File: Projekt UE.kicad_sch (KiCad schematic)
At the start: 62 parts, among them J1 NEB_21_R, J2 502382-0670, J3 TB006-508-12BE, J4 1935187, J5 215297-8, K1 G5LE-14 DC3, K2 G5LE-14 DC3, K3 G5LE-14 DC3, K4 G5LE-14 DC3, K5 G5LE-14 DC3, Q1 MMBT3904, Q2 MMBT3904, Q3 MMBT3904, Q4 MMBT3904, Q5 MMBT3904, SW1 SW_Push, SW2 SW_Push, SW3 SW_Push, SW4 SW_Push, SW5 SW_Push, SW6 SW_Push, U1 K815P, U2 MIC4575-3.3WU-TR, U3 K845P, U4 STM32F303K8T6, U5 ESP-12E, U6 L7824, Y1 ABM3-8.000MHZ-D2Y-T

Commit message: Update project.
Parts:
- removed K1, K2, K3, K4, K5: G5LE-14 DC3, Relay_THT:Relay_SPDT_Omron-G5LE-1, symbol Relay:G5LE-1
- removed U6: L7824, Package_TO_SOT_THT:TO-220-3_Vertical, symbol Regulator_Linear:L7824
- added K1, K2, K3, K4, K5: V23061B1007A301, SnapEDA Library:RELAY_1-1393223-7, symbol V23061B1007A301:V23061B1007A301
- added R18, R19, R20, R21, R22, R23: 560R, Resistor_SMD:R_1206_3216Metric, symbol Device:R
- C1, C2, C7, C8: footprint (none) -> Capacitor_THT:CP_Radial_D8.0mm_P3.50mm
- C10: footprint (none) -> Capacitor_THT:CP_Radial_D5.0mm_P2.00mm
- C3, C4: footprint (none) -> Capacitor_THT:C_Disc_D6.0mm_W2.5mm_P5.00mm
- C5, C6, C9: footprint (none) -> Capacitor_THT:C_Disc_D10.5mm_W5.0mm_P5.00mm
- J3: INFO (none) -> Valve conector
- J5: INFO (none) -> Nokia 5110
- L1: footprint (none) -> Inductor_THT:L_Radial_D24.4mm_P23.70mm_Murata_1400series
- R1, R10, R2, R3, R4, R5, R6, R7, R8, R9: footprint Resistor_THT:R_Bare_Metal_Element_L12.4mm_W4.8mm_P11.40mm -> Resistor_SMD:R_1206_3216Metric
- R11, R17: footprint (none) -> Resistor_SMD:R_1206_3216Metric
- R12, R13, R14, R15, R16: value 10K -> 10kR; footprint (none) -> Resistor_SMD:R_1206_3216Metric
- SW1, SW2, SW3, SW4, SW5, SW6: footprint (none) -> Button_Switch_THT:SW_Push_2P1T_Toggle_CK_PVA1xxH1xxxxxxV2
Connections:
- net +24V: now also D1.1 (K), D3.1 (K), D4.1 (K), D5.1 (K), D6.1 (K), U1.4, U3.10, U3.12, U3.14, U3.16, K1.11, K1.A1, K2.11, K2.A1, K3.11, K3.A1, K4.11, K4.A1, K5.11, K5.A1; no longer C1.1, U2.1 (VIN)
- net +3.3V: no longer D1.1 (K), D3.1 (K), D4.1 (K), D5.1 (K), D6.1 (K), U1.4, U3.10, U3.12, U3.14, U3.16
- net Down: now also R19.2; no longer SW2.2
- net Esc: now also R23.2; no longer SW6.2
- net Left: now also R20.2; no longer SW3.2
- net OK: now also R22.2; no longer SW5.2
- net Rain Sensor Power: now also K1.14
- net Right: now also R21.2; no longer SW4.2
- net Up: now also R18.2; no longer SW1.2
- net V1 Open: now also K2.14
- net V2 Open: now also K3.14
- net V3 Open: now also K4.14
- net V4 Open: now also K5.14
- net at D5.2 (A), Q4.3 (C): now also K4.A2
- net at D4.2 (A), Q3.3 (C): now also K3.A2
- net at D6.2 (A), Q5.3 (C): now also K5.A2
- net at J1.J: now also C1.1, U2.1 (VIN)
- net at D3.2 (A), Q2.3 (C): now also K2.A2
- net at D1.2 (A), Q1.3 (C): now also K1.A2
- new net: R18.1, SW1.2
- new net: R23.1, SW6.2
- new net: R21.1, SW4.2
- new net: R19.1, SW2.2
- new net: R20.1, SW3.2
- new net: R22.1, SW5.2
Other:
- moved on the sheet: C1, D3, D4, D5, Q1, SW1, SW2, SW3, SW4, SW5, SW6

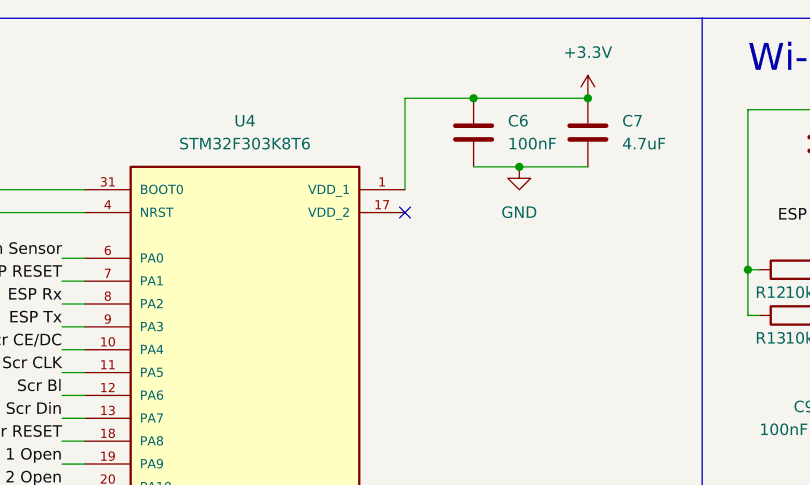
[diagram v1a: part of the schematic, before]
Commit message: Connect VDD_2 with VDD_1
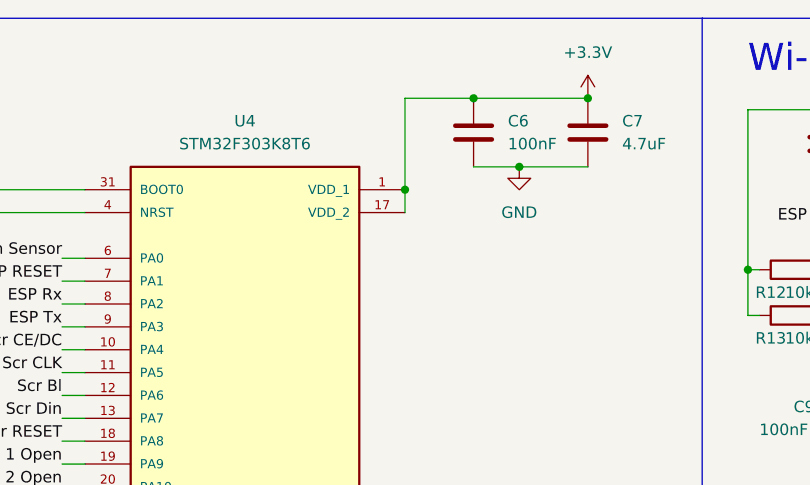
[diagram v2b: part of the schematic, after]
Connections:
- net +3.3V: now also U4.17 (VDD_2)
- no-connect marks 22 -> 21
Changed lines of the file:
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@@
   (junction (at 92.71 50.8) (diameter 0) (color 0 0 0 0)
+  )
+  (junction (at 223.52 33.02) (diameter 0) (color 0 0 0 0)
   )
   (junction (at 80.01 81.28) (diameter 0) (color 0 0 0 0)
@@
   (no_connect (at 187.96 99.06))
   (no_connect (at 223.52 88.9))
-  (no_connect (at 223.52 35.56))
   (no_connect (at 179.07 247.65))
   (no_connect (at 179.07 143.51))
@@
     (stroke (width 0) (type default) (color 0 0 0 0))
   )
+  (wire (pts (xy 223.52 33.02) (xy 223.52 35.56))
+    (stroke (width 0) (type default) (color 0 0 0 0))
+  )
